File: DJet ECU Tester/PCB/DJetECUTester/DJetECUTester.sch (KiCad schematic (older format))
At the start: 20 parts, among them J1 ISP, J2 ECU, J4 BREAKOUT, J5 12V IN, J6 MPS, U1 ATmega328P, Y1 ECS-160-18-5PX-TR 16MHz

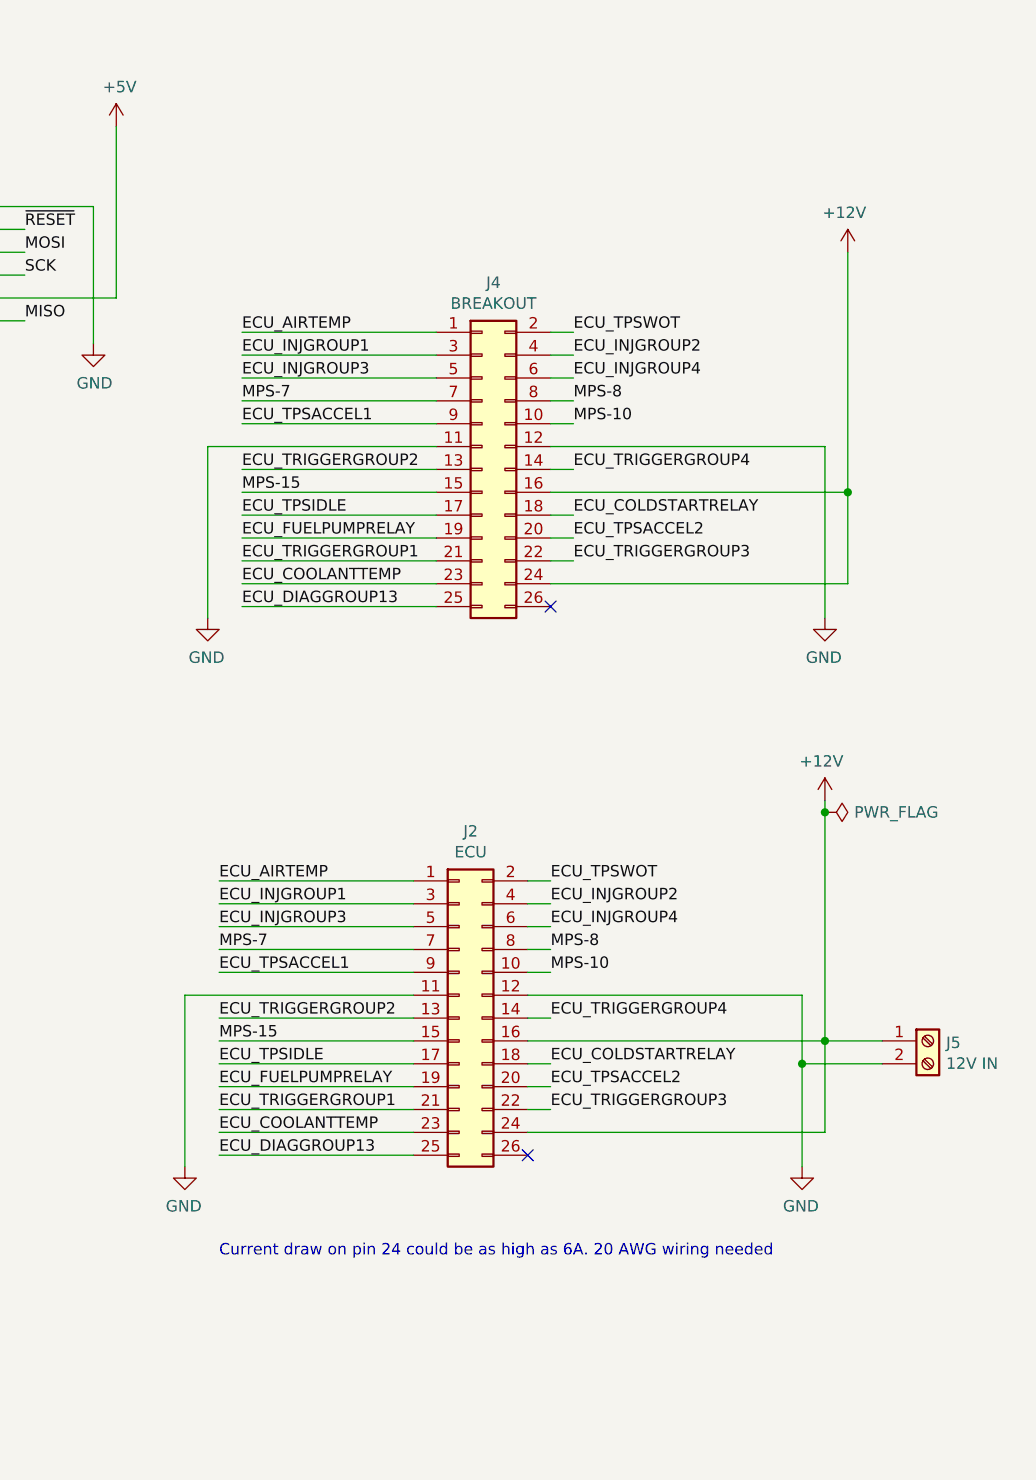
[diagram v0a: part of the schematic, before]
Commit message: Added injector waveform test points.
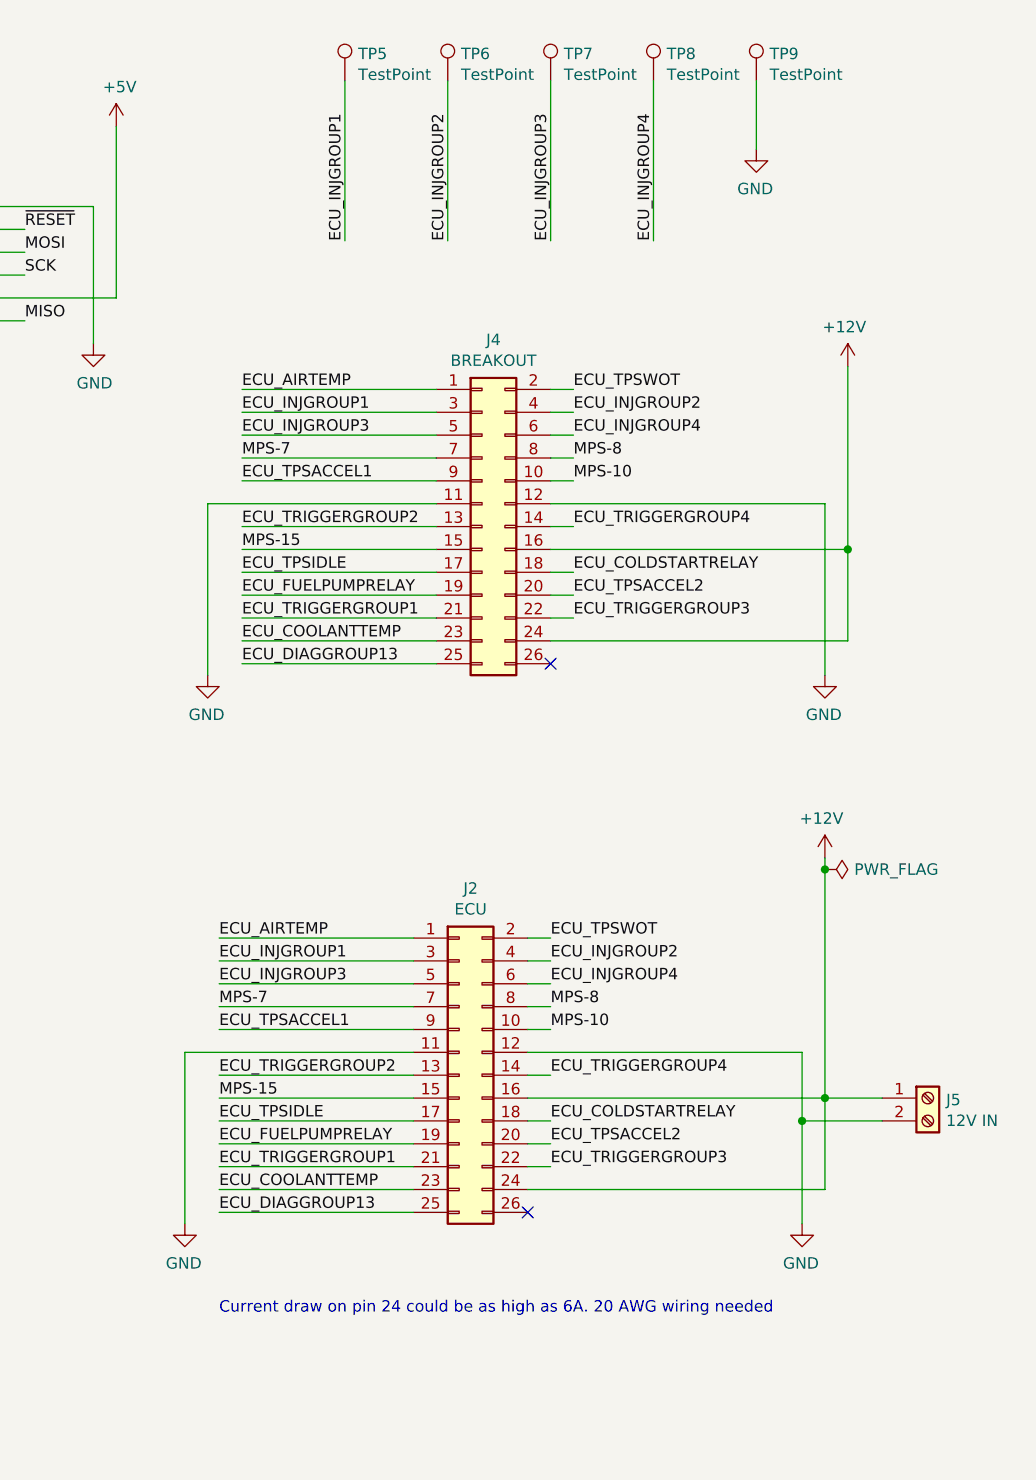
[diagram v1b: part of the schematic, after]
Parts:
- added TP5, TP6, TP7, TP8, TP9: TestPoint, symbol Connector:TestPoint
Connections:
- net ECU_INJGROUP1: now also TP5.1
- net ECU_INJGROUP2: now also TP6.1
- net ECU_INJGROUP3: now also TP7.1
- net ECU_INJGROUP4: now also TP8.1
- net GND: now also TP9.1
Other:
- moved on the sheet: J2, J4, J5

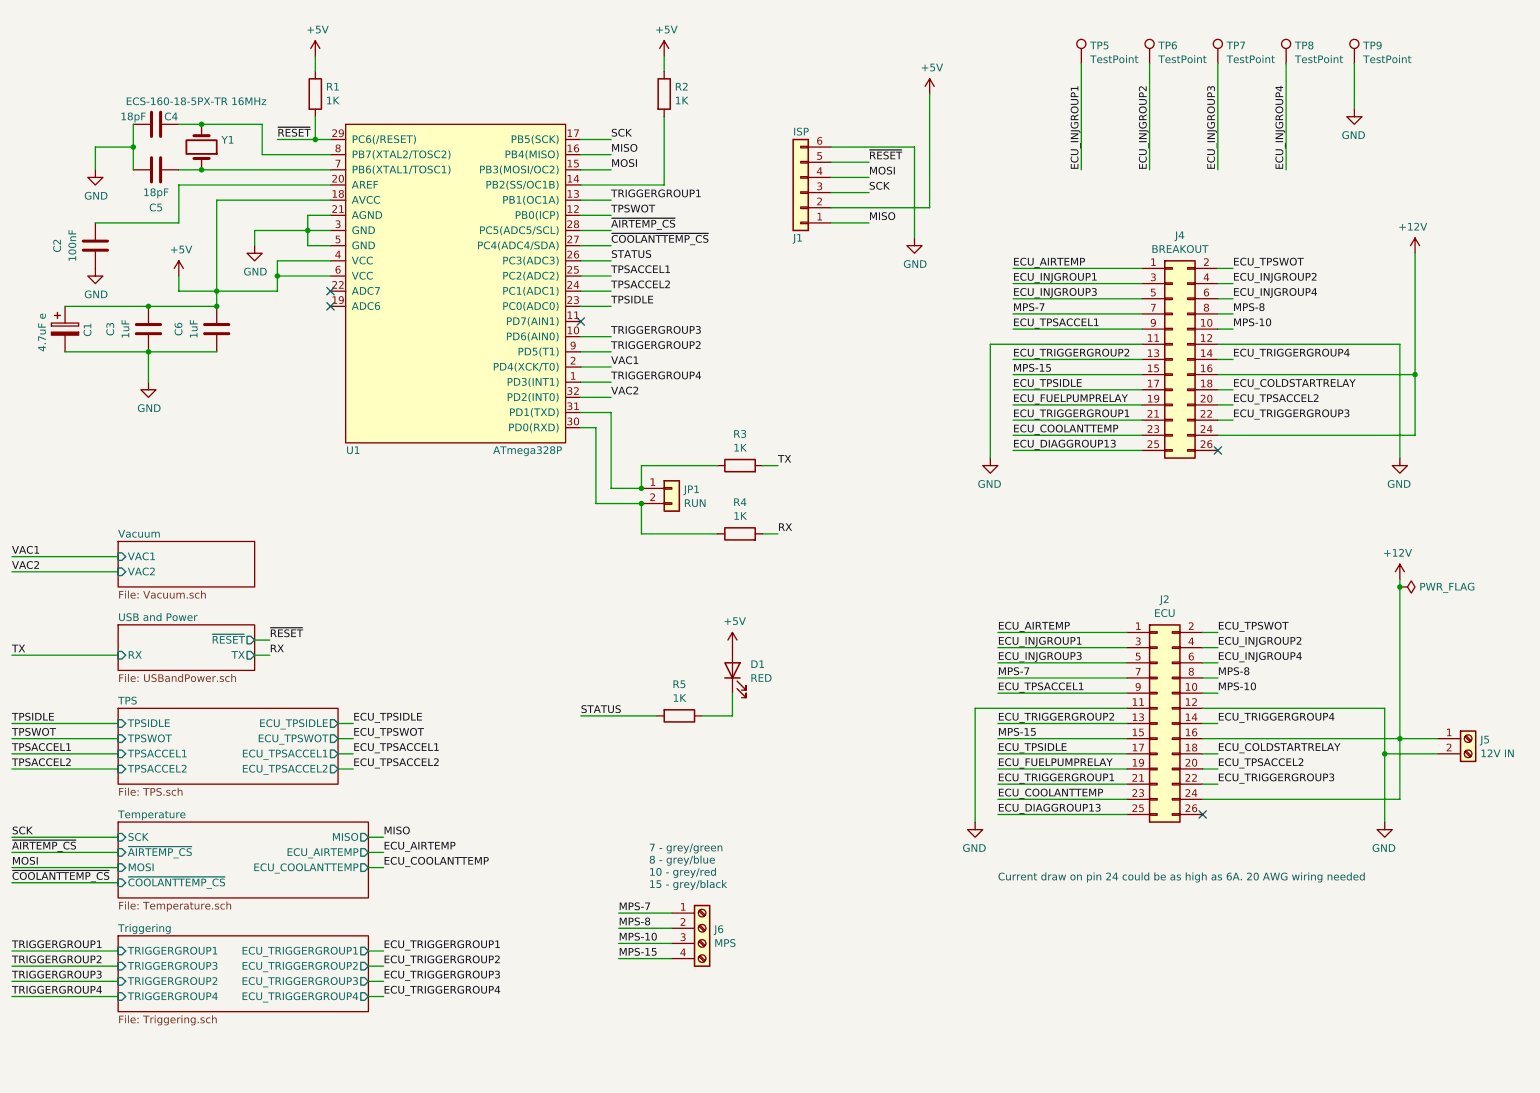
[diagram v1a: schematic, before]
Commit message: Working on ECU tester and ECU outputs board.
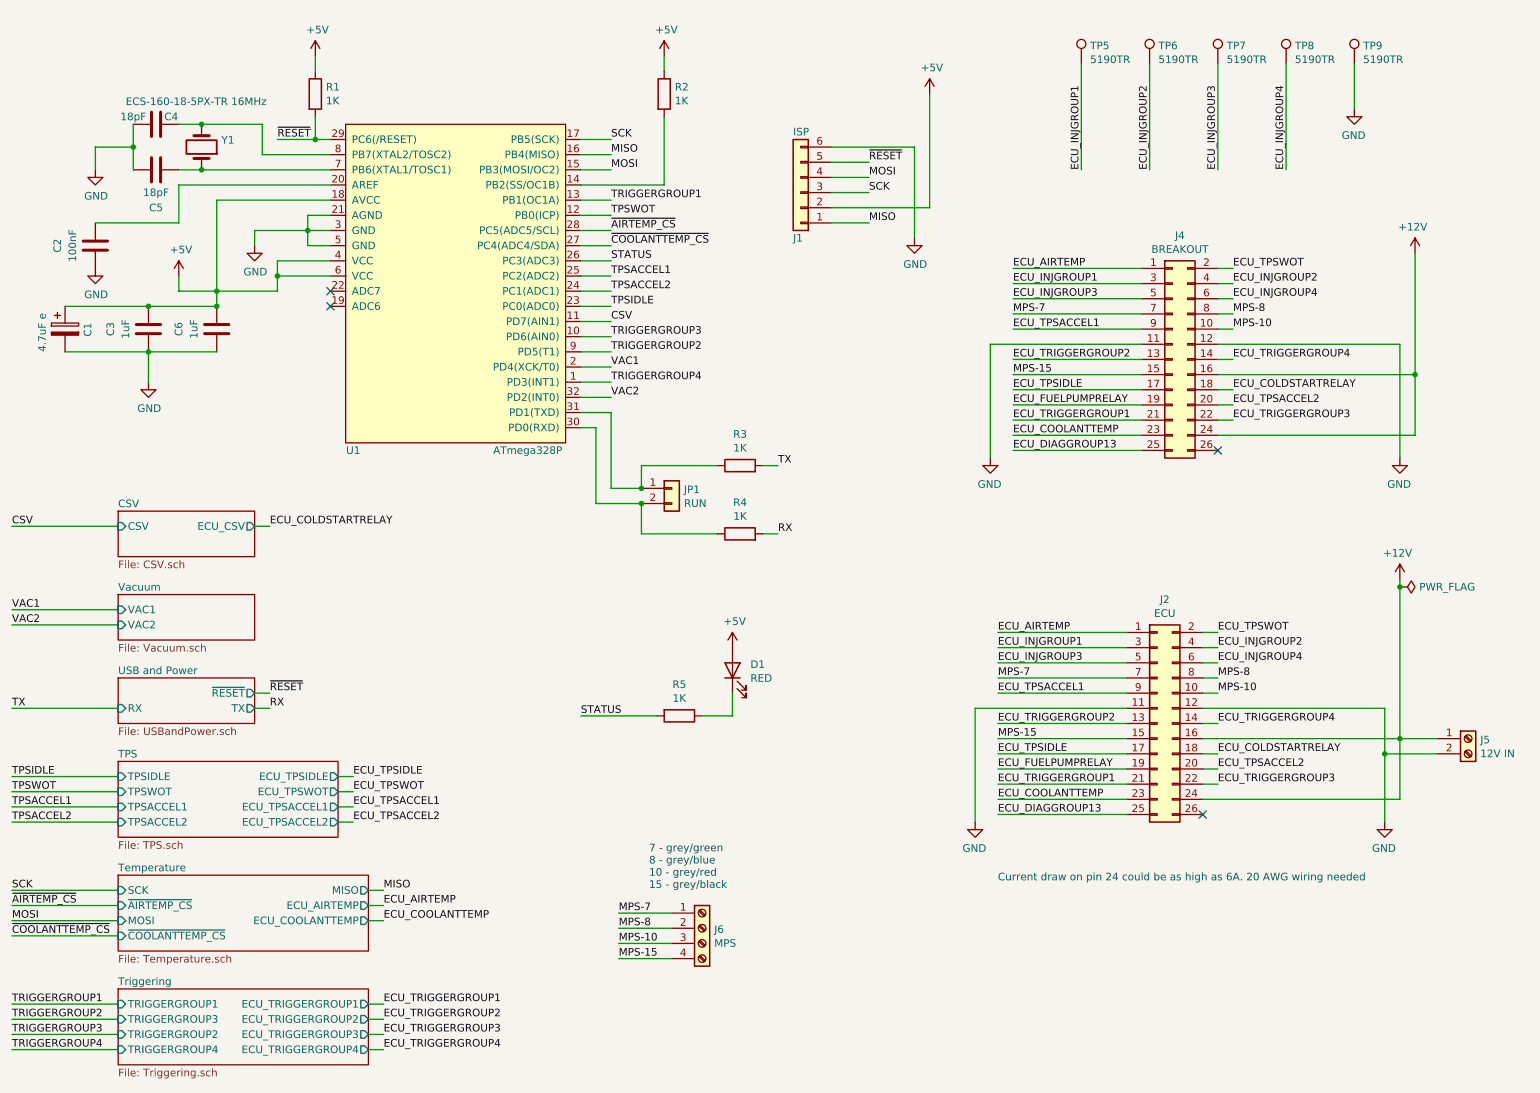
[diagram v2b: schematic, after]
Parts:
- J5: footprint (none) -> TerminalBlock_TE-Connectivity:TerminalBlock_TE_282834-2_1x02_P2.54mm_Horizontal; manf# (none) -> 282834-2
- J6: footprint (none) -> TerminalBlock_TE-Connectivity:TerminalBlock_TE_282834-4_1x04_P2.54mm_Horizontal; manf# (none) -> 282834-4
- TP5, TP6, TP7, TP8, TP9: value TestPoint -> 5190TR; footprint (none) -> Britishideas:5190TR-Colored-Test-Point; manf# (none) -> 5190TR
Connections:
- net CSV: now reaches U1.11 (PD7(AIN1))
- no-connect marks 5 -> 4

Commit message: Working on PCB layout
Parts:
- removed Y1: ECS-160-18-5PX-TR 16MHz, Britishideas:HC-49_US, symbol Device:Crystal
- added Y1: FA-238 16.0000MB-C3, Britishideas:FA-238, symbol Device:Crystal_GND24
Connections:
- net GND: now also Y1.2, Y1.4
- net at C5.2, U1.7 (PB6(XTAL1/TOSC1)): now also Y1.3
- net at C4.1, U1.8 (PB7(XTAL2/TOSC2)): now also Y1.1
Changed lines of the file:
@@
 	1    0    0    -1
 $EndComp
-$Comp
-L Device:Crystal Y1
-U 1 1 5FE96DA0
-P 2050 1450
-F 0 "Y1" V 2096 1581 50  0000 L CNN
-F 1 "ECS-160-18-5PX-TR 16MHz" V 2350 950 50  0000 L CNN
-F 2 "Britishideas:HC-49_US" H 2050 1450 50  0001 C CNN
-F 3 "~" H 2050 1450 50  0001 C CNN
-	1    2050 1450
-	0    1    -1   0
-$EndComp
-Wire Wire Line
-	2900 1600 2050 1600
 Wire Wire Line
 	2900 1500 2450 1500
 Wire Wire Line
 	2450 1500 2450 1300
-Wire Wire Line
-	2450 1300 2050 1300
 $Comp
 L Device:C C4
@@
 	0    -1   1    0
 $EndComp
-Wire Wire Line
-	1900 1300 2050 1300
-Connection ~ 2050 1300
-Wire Wire Line
-	1900 1600 2050 1600
-Connection ~ 2050 1600
 Wire Wire Line
 	1600 1300 1600 1450
@@
 Text Label 4750 2600 0    50   ~ 0
 CSV
+$Comp
+L Device:Crystal_GND24 Y1
+U 1 1 605627C0
+P 2100 1450
+F 0 "Y1" V 2054 1694 50  0000 L CNN
+F 1 "FA-238 16.0000MB-C3" V 1800 1100 50  0000 L CNN
+F 2 "Britishideas:FA-238" H 2100 1450 50  0001 C CNN
+F 3 "~" H 2100 1450 50  0001 C CNN
+F 4 "FA-238 16.0000MB-C3" H 2100 1450 50  0001 C CNN "manf#"
+	1    2100 1450
+	0    1    1    0
+$EndComp
+Wire Wire Line
+	1900 1600 2100 1600
+Wire Wire Line
+	1900 1300 2100 1300
+Connection ~ 2100 1300
+Wire Wire Line
+	2100 1300 2450 1300
+Connection ~ 2100 1600
+Wire Wire Line
+	2100 1600 2900 1600
+Wire Wire Line
+	1900 1450 1600 1450
+Wire Wire Line
+	2300 1450 2400 1450
+Wire Wire Line
+	2400 1450 2400 2000
+Connection ~ 2400 2000
 $EndSCHEMATC

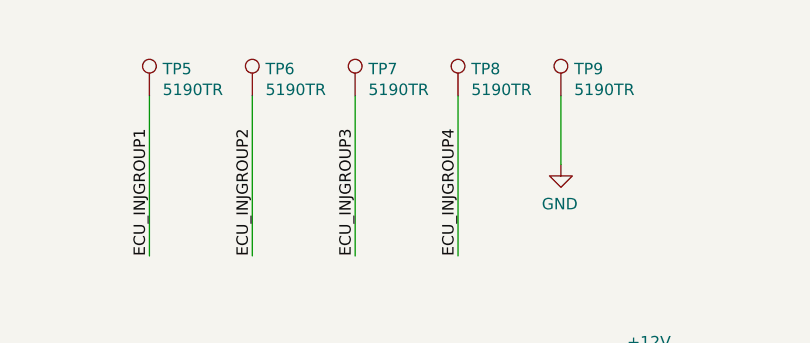
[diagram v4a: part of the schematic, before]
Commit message: Added final 3D models.
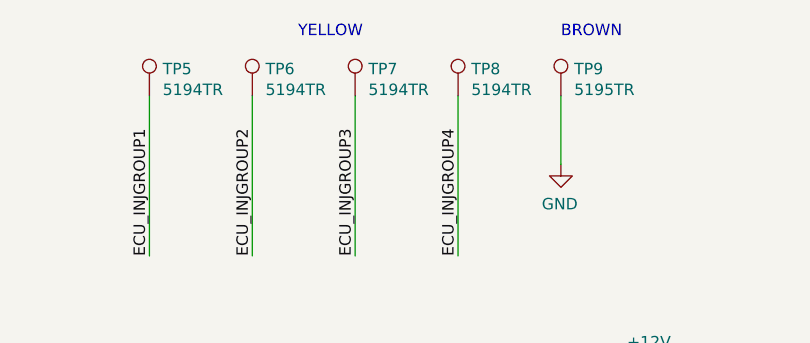
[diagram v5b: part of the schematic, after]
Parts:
- TP5, TP6, TP7, TP8: value 5190TR -> 5194TR; manf# 5190TR -> 5194TR
- TP9: value 5190TR -> 5195TR; manf# 5190TR -> 5195TR
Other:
- note added: "BROWN"
- note added: "YELLOW"
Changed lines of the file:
@@
 Sheet 1 7
 Title "D-Jetronic ECU Tester"
-Date "2021-03-09"
+Date "2021-03-12"
 Rev "1.0"
 Comp "(C) Britishideas 2021"
@@
 P 7850 900
 F 0 "TP5" H 7908 1018 50  0000 L CNN
-F 1 "5190TR" H 7908 927 50  0000 L CNN
+F 1 "5194TR" H 7908 927 50  0000 L CNN
 F 2 "Britishideas:5190TR-Colored-Test-Point" H 8050 900 50  0001 C CNN
 F 3 "~" H 8050 900 50  0001 C CNN
-F 4 "5190TR" H 7850 900 50  0001 C CNN "manf#"
+F 4 "5194TR" H 7850 900 50  0001 C CNN "manf#"
 	1    7850 900
 	1    0    0    -1
@@
 P 8300 900
 F 0 "TP6" H 8358 1018 50  0000 L CNN
-F 1 "5190TR" H 8358 927 50  0000 L CNN
+F 1 "5194TR" H 8358 927 50  0000 L CNN
 F 2 "Britishideas:5190TR-Colored-Test-Point" H 8500 900 50  0001 C CNN
 F 3 "~" H 8500 900 50  0001 C CNN
-F 4 "5190TR" H 8300 900 50  0001 C CNN "manf#"
+F 4 "5194TR" H 8300 900 50  0001 C CNN "manf#"
 	1    8300 900
 	1    0    0    -1
@@
 P 8750 900
 F 0 "TP7" H 8808 1018 50  0000 L CNN
-F 1 "5190TR" H 8808 927 50  0000 L CNN
+F 1 "5194TR" H 8808 927 50  0000 L CNN
 F 2 "Britishideas:5190TR-Colored-Test-Point" H 8950 900 50  0001 C CNN
 F 3 "~" H 8950 900 50  0001 C CNN
-F 4 "5190TR" H 8750 900 50  0001 C CNN "manf#"
+F 4 "5194TR" H 8750 900 50  0001 C CNN "manf#"
 	1    8750 900
 	1    0    0    -1
@@
 P 9200 900
 F 0 "TP8" H 9258 1018 50  0000 L CNN
-F 1 "5190TR" H 9258 927 50  0000 L CNN
+F 1 "5194TR" H 9258 927 50  0000 L CNN
 F 2 "Britishideas:5190TR-Colored-Test-Point" H 9400 900 50  0001 C CNN
 F 3 "~" H 9400 900 50  0001 C CNN
-F 4 "5190TR" H 9200 900 50  0001 C CNN "manf#"
+F 4 "5194TR" H 9200 900 50  0001 C CNN "manf#"
 	1    9200 900
 	1    0    0    -1
@@
 P 9650 900
 F 0 "TP9" H 9708 1018 50  0000 L CNN
-F 1 "5190TR" H 9708 927 50  0000 L CNN
+F 1 "5195TR" H 9708 927 50  0000 L CNN
 F 2 "Britishideas:5190TR-Colored-Test-Point" H 9850 900 50  0001 C CNN
 F 3 "~" H 9850 900 50  0001 C CNN
-F 4 "5190TR" H 9650 900 50  0001 C CNN "manf#"
+F 4 "5195TR" H 9650 900 50  0001 C CNN "manf#"
 	1    9650 900
 	1    0    0    -1
@@
 	2400 1450 2400 2000
 Connection ~ 2400 2000
+Text Notes 9650 650  0    50   ~ 0
+BROWN
+Text Notes 8500 650  0    50   ~ 0
+YELLOW
 $EndSCHEMATC
